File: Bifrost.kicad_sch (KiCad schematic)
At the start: 58 parts, among them J1 OIP, J2 Conn_01x03_Male, J3 Conn_01x03_Male, U3 LMH6881

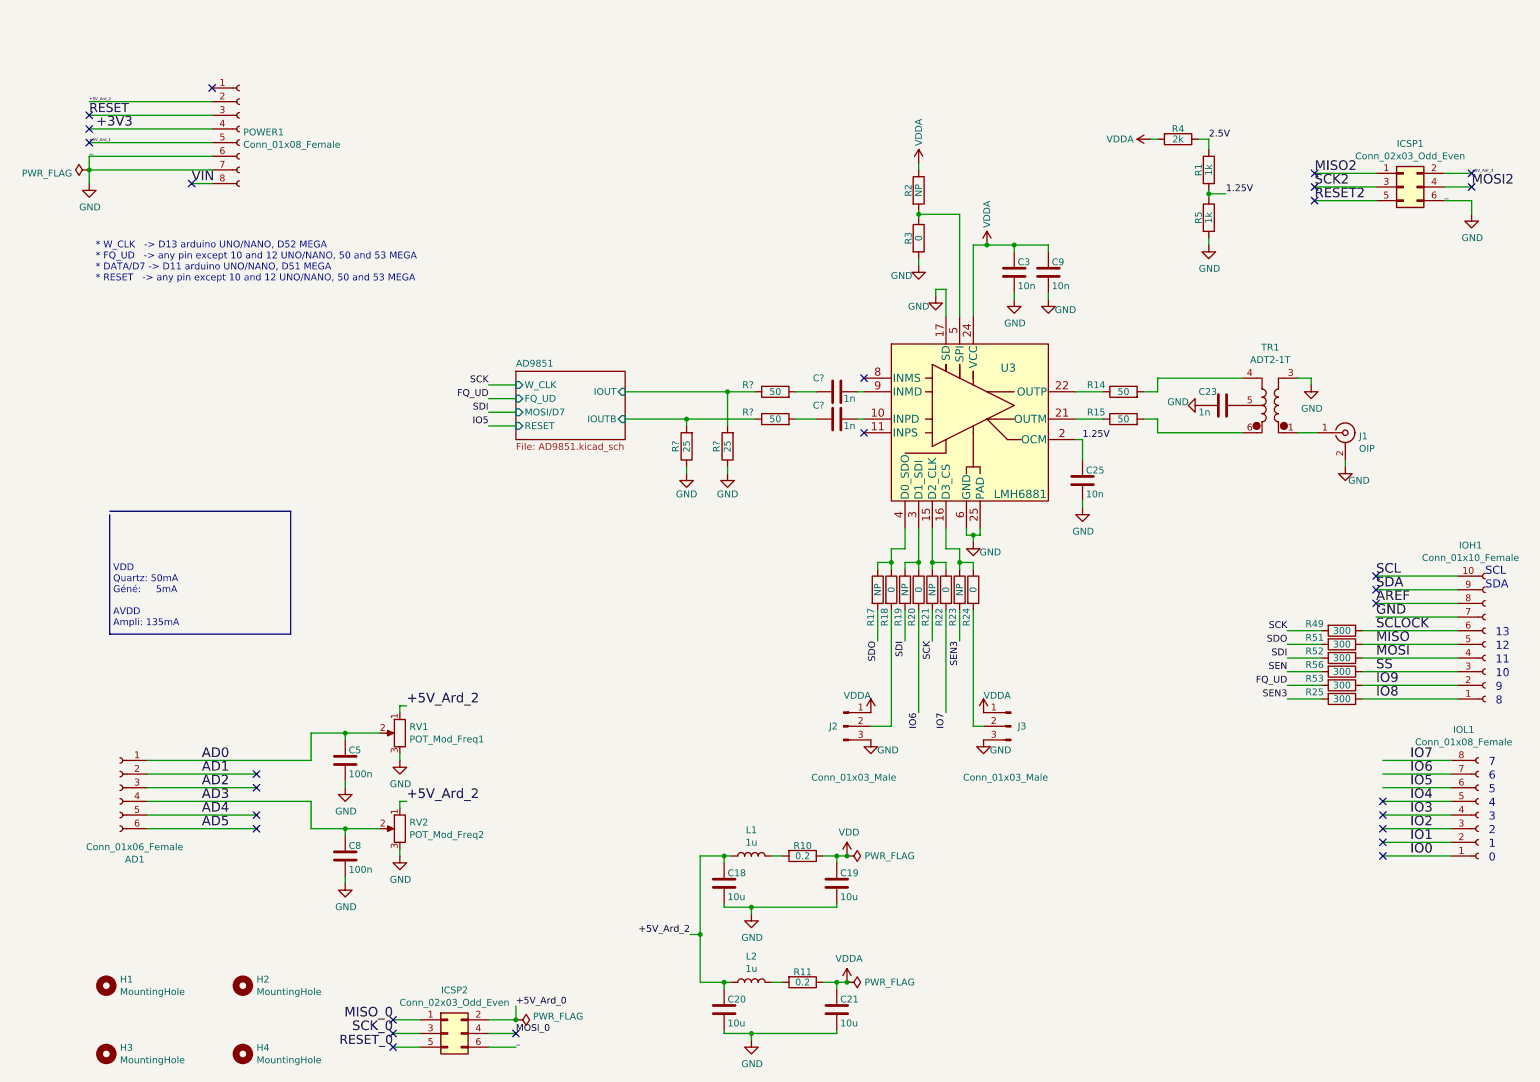
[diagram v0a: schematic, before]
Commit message: Added filters on output wired the option to have all of the amplifier parallel bits connected
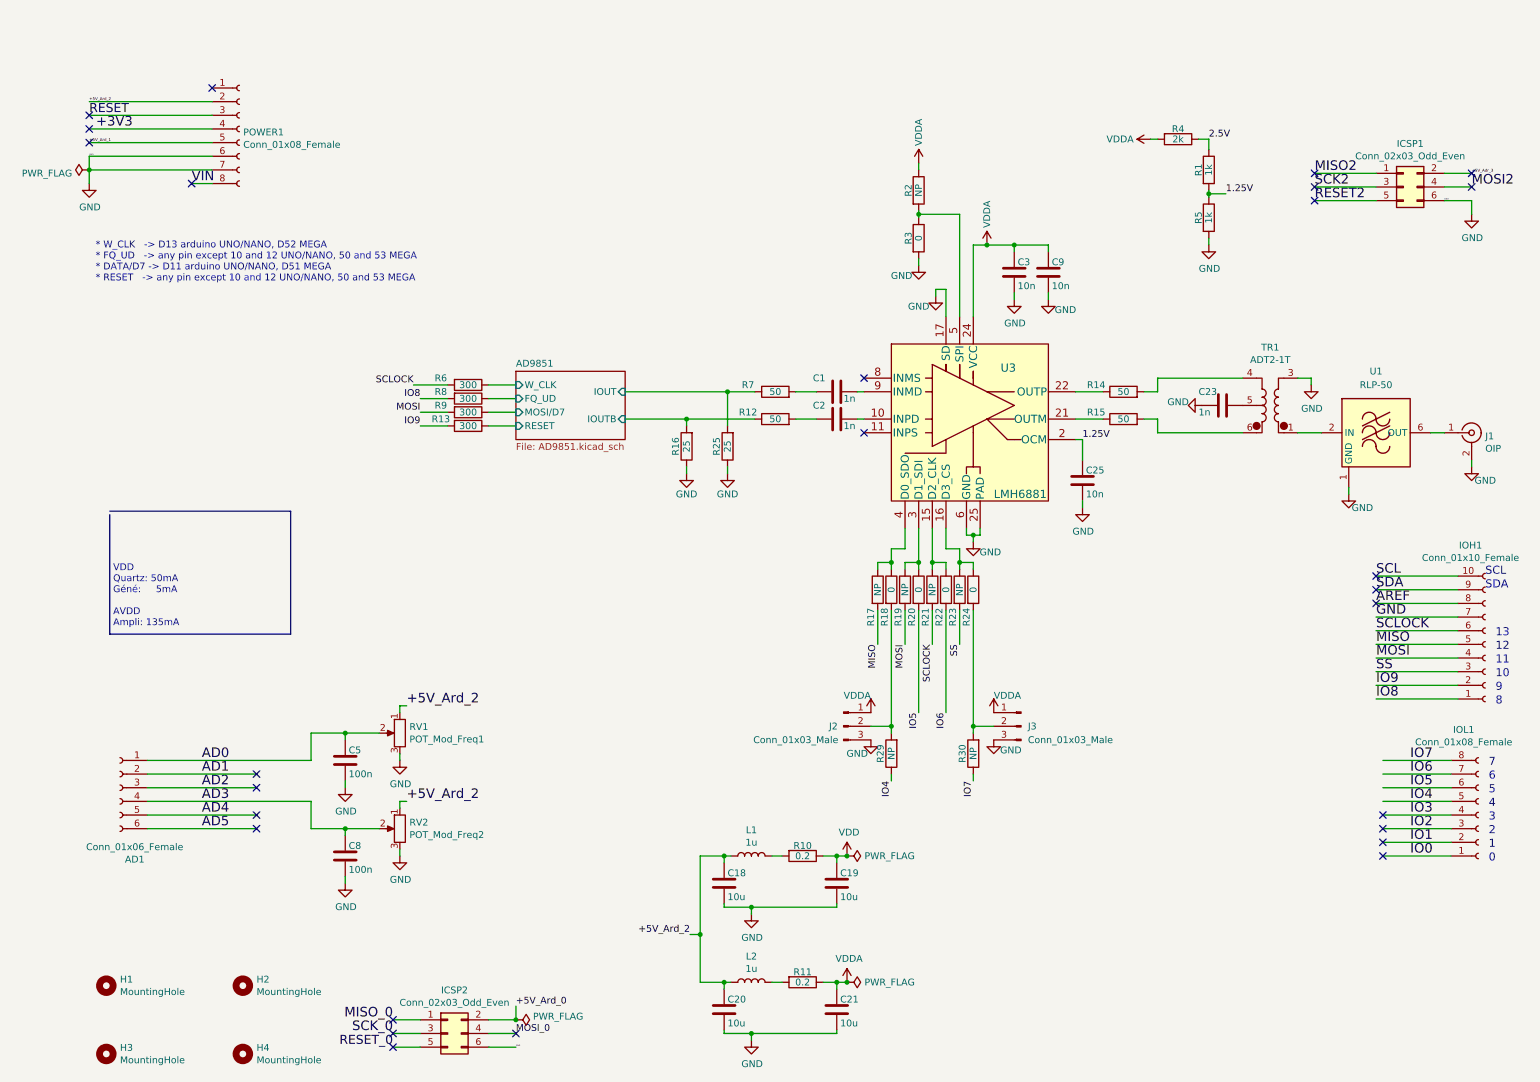
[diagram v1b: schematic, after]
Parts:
- removed R25, R49, R51, R52, R53, R56: 300, Resistor_SMD:R_0603_1608Metric_Pad0.98x0.95mm_HandSolder, symbol Device:R
- added R13, R6, R8, R9: 300, Resistor_SMD:R_0603_1608Metric_Pad0.98x0.95mm_HandSolder, symbol Device:R
- added R29, R30: NP, Resistor_SMD:R_0603_1608Metric_Pad0.98x0.95mm_HandSolder, symbol Device:R
- added U1: RLP-50, RF_Mini-Circuits:Mini-Circuits_GP1212_LandPatternPL-176, symbol RF_Filter:RLP-30
- R16, R25: renamed from R?; footprint (none) -> Resistor_SMD:R_0603_1608Metric_Pad0.98x0.95mm_HandSolder
- RV1, RV2: symbol Device:R_POT -> Device:R_Potentiometer
- gave numbers to parts that had none: 4
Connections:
- net SCK is gone; now on net SCLOCK: R21.2
- net SDI is gone; now on net MOSI: R19.2
- net SDO is gone; now on net MISO: R17.2
- net SEN3 is gone; now on net SS: R23.2
- net GND: now also U1.1 (GND), U1.3 (GND), U1.4 (GND), U1.5 (GND), U1.7 (GND), U1.8 (GND)
- net IO4: now also R29.1
- net IO5: now also R20.2
- net IO6: now also R22.2; no longer R20.2
- net IO7: now also R30.1; no longer R22.2
- net IO8: now also R8.2
- net IO9: now also R13.2
- net MOSI: now also R9.2
- net SCLOCK: now also R6.2
- net at J1.1 (In): now also U1.6 (OUT); no longer TR1.1
- net at J2.2 (Pin_2), R18.2: now also R29.2
- net at J3.2 (Pin_2), R24.2: now also R30.2
- new net: TR1.1, U1.2 (IN)
- new net AD9851/FQ_UD: R8.1
- new net AD9851/MOSI/D7: R9.1
- new net AD9851/RESET: R13.1
- new net AD9851/W_CLK: R6.1
- no-connect marks 28 -> 27
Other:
- moved on the sheet: J1, J3

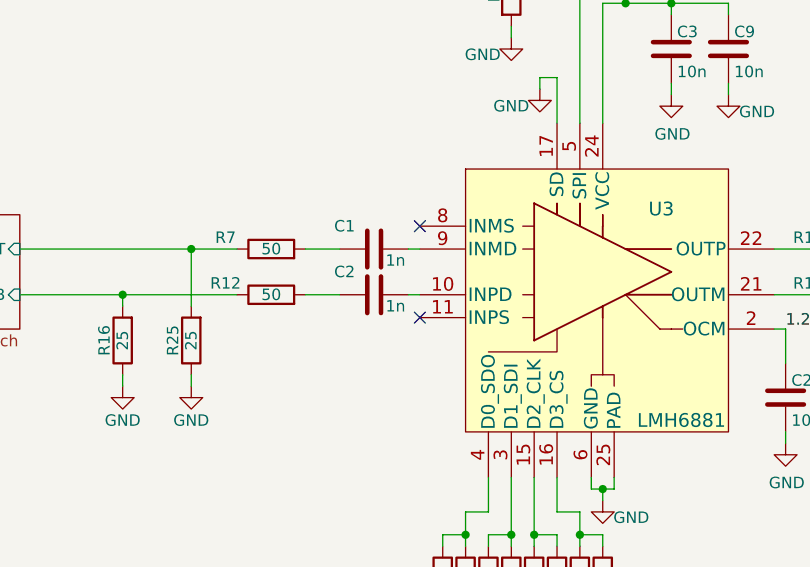
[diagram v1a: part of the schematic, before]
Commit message: Finished serigraphie IBOM generated and components sourced
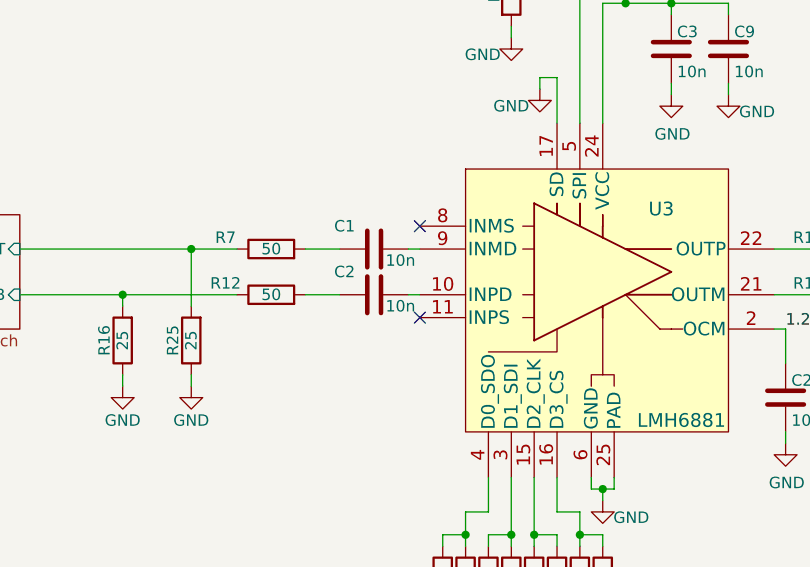
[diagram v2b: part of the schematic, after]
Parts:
- C1, C2: value 1n -> 10n
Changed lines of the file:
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@@
       (effects (font (size 1.27 1.27)) (justify right))
     )
-    (property "Value" "1n" (id 1) (at 154.94 72.39 90)
+    (property "Value" "10n" (id 1) (at 154.94 72.39 90)
       (effects (font (size 1.27 1.27)) (justify right))
     )
@@
       (effects (font (size 1.27 1.27)) (justify right))
     )
-    (property "Value" "1n" (id 1) (at 154.94 77.47 90)
+    (property "Value" "10n" (id 1) (at 154.94 77.47 90)
       (effects (font (size 1.27 1.27)) (justify right))
     )
@@
     )
     (path "/00f3d2c9-0a01-4d63-befb-f2061e1d4edb"
-      (reference "C1") (unit 1) (value "1n") (footprint "Capacitor_SMD:C_0603_1608Metric_Pad1.08x0.95mm_HandSolder")
+      (reference "C1") (unit 1) (value "10n") (footprint "Capacitor_SMD:C_0603_1608Metric_Pad1.08x0.95mm_HandSolder")
     )
     (path "/01e220c1-f50b-4aa5-8c5b-e2610f2347fc"
-      (reference "C2") (unit 1) (value "1n") (footprint "Capacitor_SMD:C_0603_1608Metric_Pad1.08x0.95mm_HandSolder")
+      (reference "C2") (unit 1) (value "10n") (footprint "Capacitor_SMD:C_0603_1608Metric_Pad1.08x0.95mm_HandSolder")
     )
     (path "/00000000-0000-0000-0000-0000617193a6"

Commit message: As implemented
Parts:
- R29: value NP -> (none); footprint Resistor_SMD:R_0603_1608Metric_Pad0.98x0.95mm_HandSolder -> (none)
- R30: value NP -> (none)
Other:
- note added: "NP"
- note added: "https://comus-intl.com/wp-content/uploads/2015/01/3570-1412-Series.pdf"
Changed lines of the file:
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@@
     (effects (font (size 1.4986 1.4986)) (justify left bottom))
+  )
+  (text "NP" (at 160.02 133.35 0)
+    (effects (font (size 1.27 1.27)) (justify left bottom))
   )
   (text "2" (at 274.955 153.67 0)
     (effects (font (size 1.4986 1.4986)) (justify left bottom))
+  )
+  (text "https://comus-intl.com/wp-content/uploads/2015/01/3570-1412-Series.pdf"
+    (at 0 2.54 0)
+    (effects (font (size 1.27 1.27)) (justify left bottom))
   )
   (text "1" (at 274.955 156.21 0)
@@
   (text "6" (at 274.955 143.51 0)
     (effects (font (size 1.4986 1.4986)) (justify left bottom))
+  )
+  (text "NP" (at 180.34 133.35 0)
+    (effects (font (size 1.27 1.27)) (justify left bottom))
   )
   (text "12" (at 276.225 119.38 0)
@@
     (in_bom yes) (on_board yes)
     (property "Reference" "R30" (id 0) (at 177.038 138.43 90))
-    (property "Value" "NP" (id 1) (at 179.07 138.43 90))
+    (property "Value" "" (id 1) (at 179.07 138.43 90))
     (property "Footprint" "Resistor_SMD:R_0603_1608Metric_Pad0.98x0.95mm_HandSolder" (id 2) (at 180.848 138.43 90)
       (effects (font (size 1.27 1.27)) hide)
@@
     (in_bom yes) (on_board yes)
     (property "Reference" "R29" (id 0) (at 161.798 138.43 90))
-    (property "Value" "NP" (id 1) (at 163.83 138.43 90))
-    (property "Footprint" "Resistor_SMD:R_0603_1608Metric_Pad0.98x0.95mm_HandSolder" (id 2) (at 165.608 138.43 90)
+    (property "Value" "" (id 1) (at 163.83 138.43 90))
+    (property "Footprint" "" (id 2) (at 165.608 138.43 90)
       (effects (font (size 1.27 1.27)) hide)
     )
@@
     )
     (path "/e8ceb33b-b7d8-4507-aac9-886c6a938404"
-      (reference "R29") (unit 1) (value "NP") (footprint "Resistor_SMD:R_0603_1608Metric_Pad0.98x0.95mm_HandSolder")
+      (reference "R29") (unit 1) (value "0") (footprint "Resistor_SMD:R_0603_1608Metric_Pad0.98x0.95mm_HandSolder")
     )
     (path "/b5c3c647-8af2-4447-b39c-08ed01ecab14"
-      (reference "R30") (unit 1) (value "NP") (footprint "Resistor_SMD:R_0603_1608Metric_Pad0.98x0.95mm_HandSolder")
+      (reference "R30") (unit 1) (value "0") (footprint "Resistor_SMD:R_0603_1608Metric_Pad0.98x0.95mm_HandSolder")
     )
     (path "/00000000-0000-0000-0000-000061004d85"

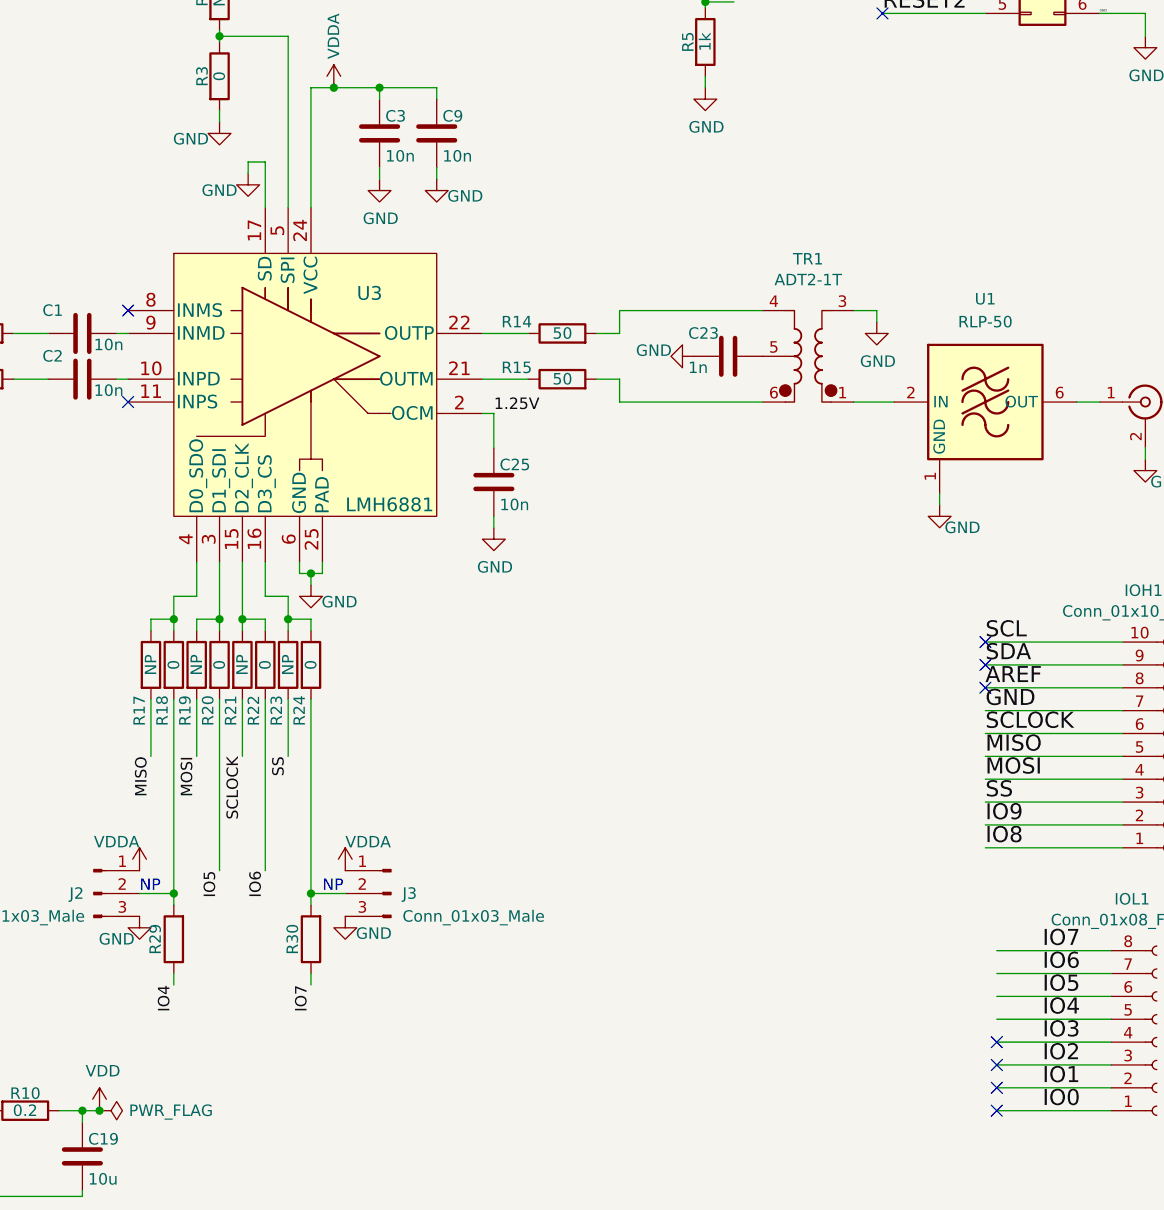
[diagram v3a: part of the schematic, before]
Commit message: Connected ampli's ShutDown pin
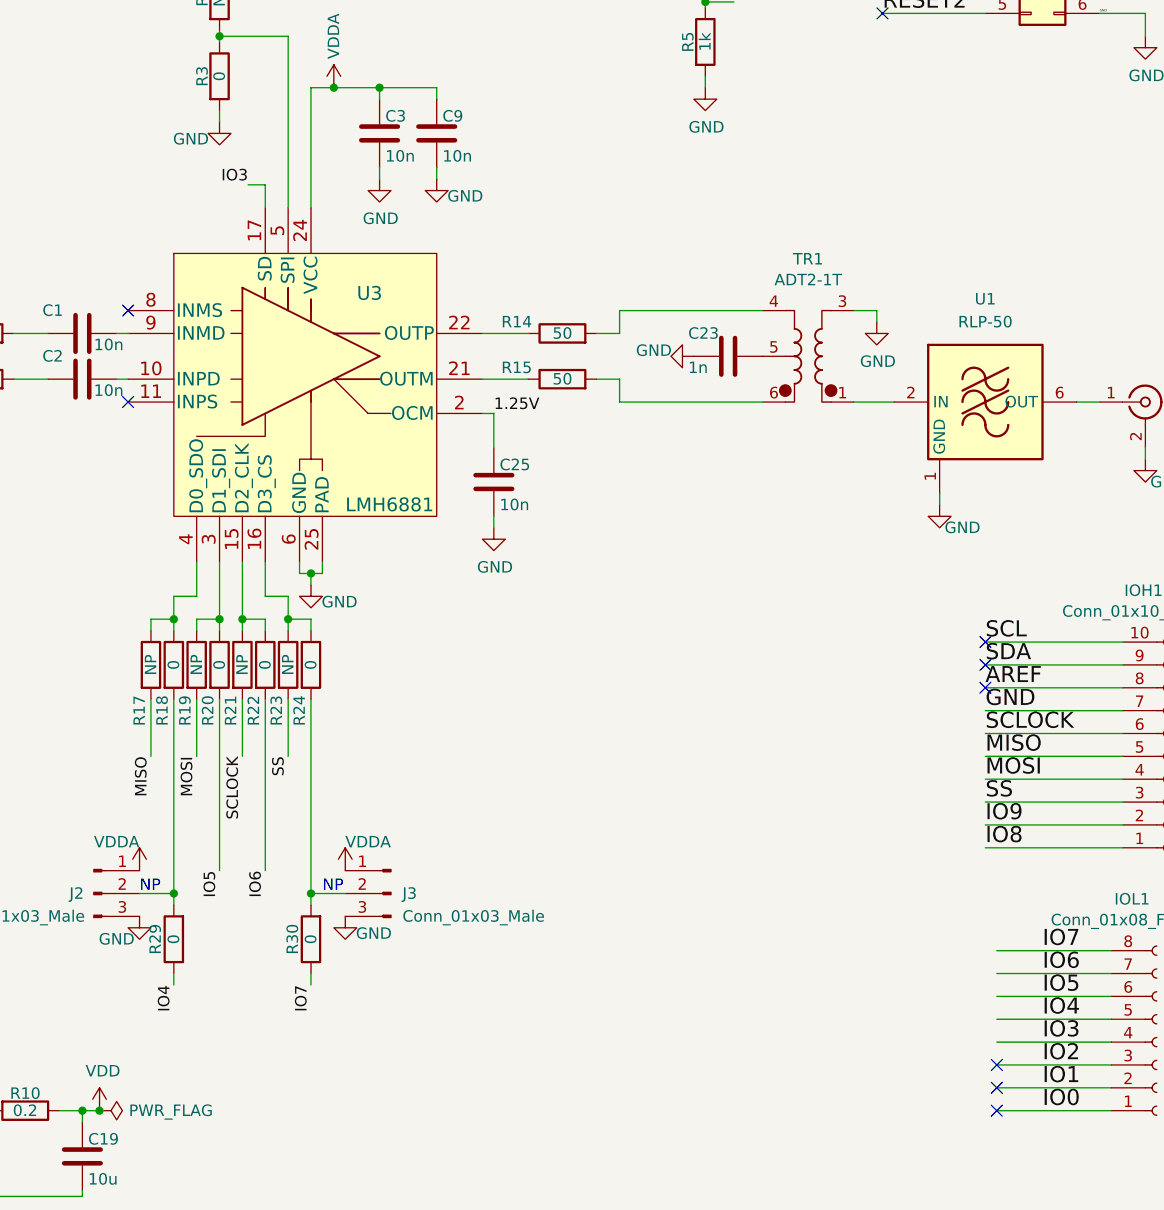
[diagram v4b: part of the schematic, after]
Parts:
- R29: value (none) -> 0; footprint (none) -> Resistor_SMD:R_0603_1608Metric_Pad0.98x0.95mm_HandSolder
- R30: value (none) -> 0
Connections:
- net GND: no longer U3.17 (SD)
- net IO3: now also U3.17 (SD)
- no-connect marks 27 -> 26
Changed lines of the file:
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@@
   (no_connect (at 45.72 152.4))
   (no_connect (at 255.27 152.4))
-  (no_connect (at 255.27 149.86))
   (no_connect (at 158.75 68.58))
   (no_connect (at 158.75 78.74))
@@
     (stroke (width 0) (type default) (color 0 0 0 0))
   )
-  (wire (pts (xy 173.99 52.07) (xy 173.99 57.15))
+  (wire (pts (xy 173.99 54.61) (xy 173.99 57.15))
     (stroke (width 0) (type default) (color 0 0 0 0))
   )
@@
     (stroke (width 0) (type default) (color 0 0 0 0))
   )
-  (wire (pts (xy 172.085 52.07) (xy 173.99 52.07))
+  (wire (pts (xy 172.085 54.61) (xy 173.99 54.61))
     (stroke (width 0) (type default) (color 0 0 0 0))
   )
@@
   )
   (wire (pts (xy 62.23 134.62) (xy 68.58 134.62))
-    (stroke (width 0) (type default) (color 0 0 0 0))
-  )
-  (wire (pts (xy 172.085 52.07) (xy 172.085 53.34))
     (stroke (width 0) (type default) (color 0 0 0 0))
   )
@@
   )
   (label "IO7" (at 179.07 143.51 270)
+    (effects (font (size 1.27 1.27)) (justify right bottom))
+  )
+  (label "IO3" (at 172.085 54.61 180)
     (effects (font (size 1.27 1.27)) (justify right bottom))
   )
@@
     (pin "2")
   )
-  (symbol (lib_id "power:GND") (at 172.085 53.34 0) (unit 1)
-    (in_bom yes) (on_board yes)
-    (property "Reference" "#PWR037" (id 0) (at 172.085 59.69 0)
-      (effects (font (size 1.27 1.27)) hide)
-    )
-    (property "Value" "GND" (id 1) (at 168.91 55.245 0))
-    (property "Footprint" "" (id 2) (at 172.085 53.34 0)
-      (effects (font (size 1.27 1.27)) hide)
-    )
-    (property "Datasheet" "" (id 3) (at 172.085 53.34 0)
-      (effects (font (size 1.27 1.27)) hide)
-    )
-    (pin "1")
-  )
   (symbol (lib_id "Device:R") (at 168.91 42.545 0) (unit 1)
     (in_bom yes) (on_board yes)
@@
     (in_bom yes) (on_board yes)
     (property "Reference" "R30" (id 0) (at 177.038 138.43 90))
-    (property "Value" "" (id 1) (at 179.07 138.43 90))
+    (property "Value" "0" (id 1) (at 179.07 138.43 90))
     (property "Footprint" "Resistor_SMD:R_0603_1608Metric_Pad0.98x0.95mm_HandSolder" (id 2) (at 180.848 138.43 90)
       (effects (font (size 1.27 1.27)) hide)
@@
     (in_bom yes) (on_board yes)
     (property "Reference" "R29" (id 0) (at 161.798 138.43 90))
-    (property "Value" "" (id 1) (at 163.83 138.43 90))
-    (property "Footprint" "" (id 2) (at 165.608 138.43 90)
+    (property "Value" "0" (id 1) (at 163.83 138.43 90))
+    (property "Footprint" "Resistor_SMD:R_0603_1608Metric_Pad0.98x0.95mm_HandSolder" (id 2) (at 165.608 138.43 90)
       (effects (font (size 1.27 1.27)) hide)
     )
@@
       (reference "#PWR036") (unit 1) (value "GND") (footprint "")
     )
-    (path "/00000000-0000-0000-0000-0000618e8b8e"
-      (reference "#PWR037") (unit 1) (value "GND") (footprint "")
-    )
     (path "/00000000-0000-0000-0000-00006169bf9f"
